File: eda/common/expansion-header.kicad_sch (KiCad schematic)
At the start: 10 parts, among them J1 Bus expansion

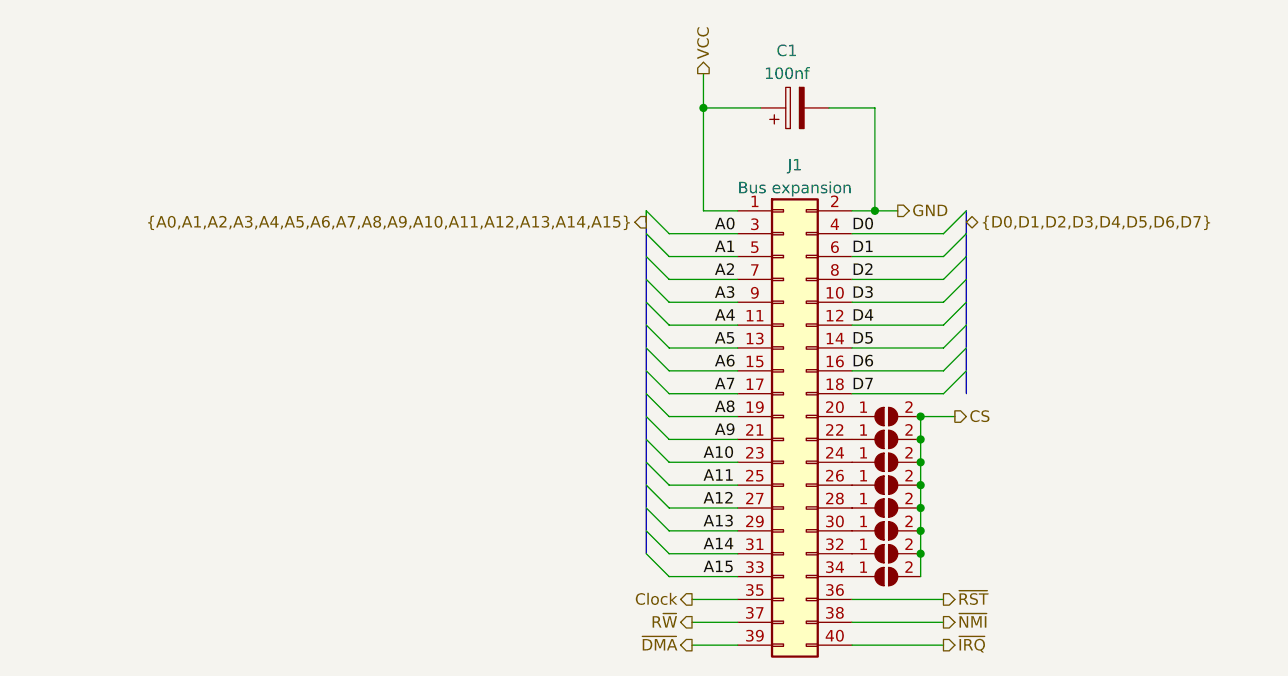
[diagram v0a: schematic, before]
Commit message: More work on UART
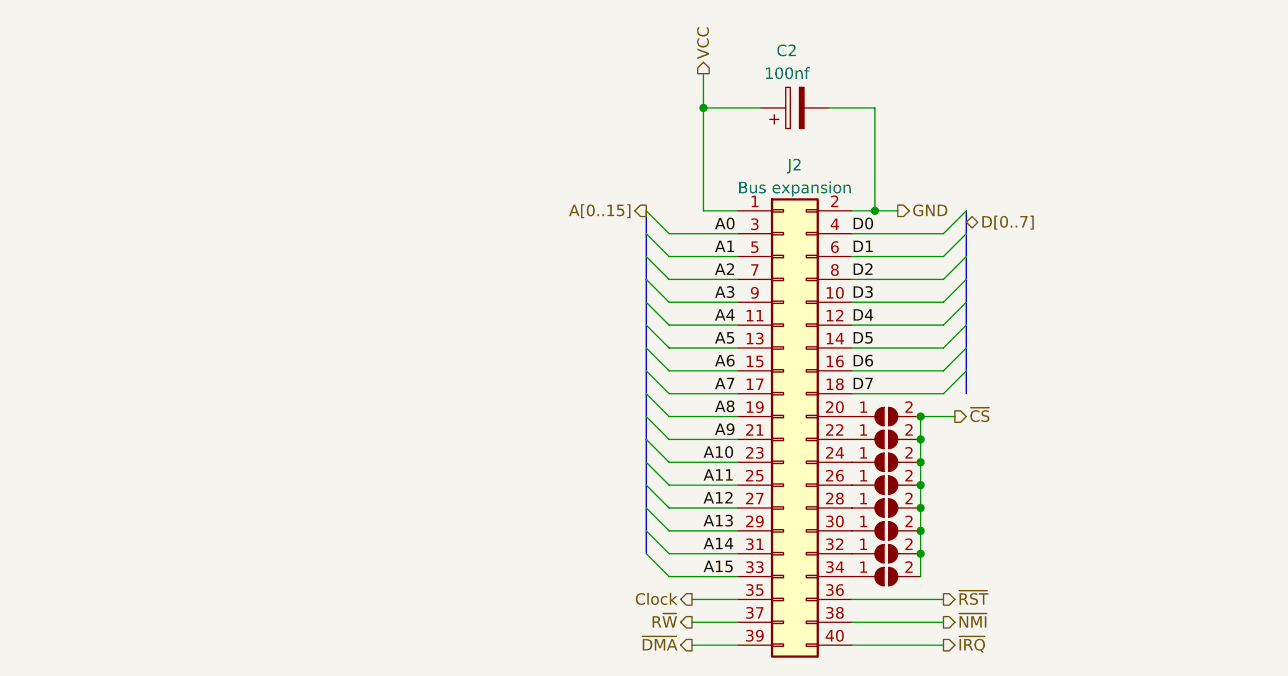
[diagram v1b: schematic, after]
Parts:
- renumbered C1 to C2, J1 to J2
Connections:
- net CS renamed ~{CS}

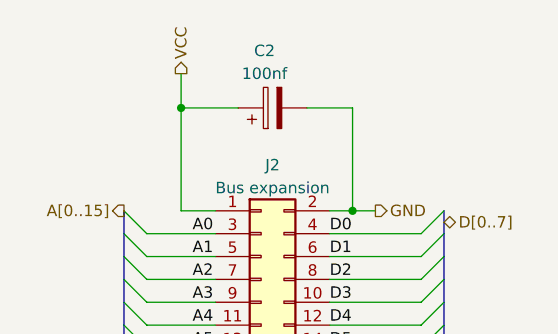
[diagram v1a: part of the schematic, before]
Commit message: Port main board schematic to kicad
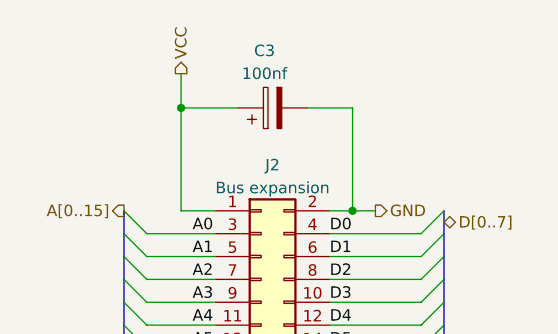
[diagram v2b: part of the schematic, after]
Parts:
- renumbered C2 to C3
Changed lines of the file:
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@@
   (symbol (lib_id "Device:C_Polarized") (at 90.17 38.1 90) (unit 1)
     (in_bom yes) (on_board yes) (dnp no) (fields_autoplaced)
-    (property "Reference" "C2" (at 89.281 31.75 90)
+    (property "Reference" "C3" (at 89.281 31.75 90)
       (effects (font (size 1.27 1.27)))
     )
@@
       (project "uart"
         (path "/11545594-d6d6-4b37-a578-fa23933d5773/07300109-a3a2-4acb-97d9-cd917026a3f9"
-          (reference "C2") (unit 1)
+          (reference "C3") (unit 1)
         )
       )

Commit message: Work on main board eda, interim
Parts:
- renumbered C3 to C18
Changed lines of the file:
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@@
     (pin "9")
     (instances
-      (project "uart"
-        (path "/11545594-d6d6-4b37-a578-fa23933d5773/07300109-a3a2-4acb-97d9-cd917026a3f9"
+      (project "fpga_gpu"
+        (path "/1109c9a4-a9ef-4407-8781-29fe7740bcaf/e520acf4-60a8-4598-8dc0-60738d0b1043/67c1a8cf-e42b-4097-97dd-eb2d8cef1b43"
           (reference "J2") (unit 1)
         )
       )
+      (project "uart"
+        (path "/11545594-d6d6-4b37-a578-fa23933d5773/07300109-a3a2-4acb-97d9-cd917026a3f9"
+          (reference "J2") (unit 1)
+        )
+      )
     )
   )
@@
     (pin "2")
     (instances
-      (project "uart"
-        (path "/11545594-d6d6-4b37-a578-fa23933d5773/07300109-a3a2-4acb-97d9-cd917026a3f9"
+      (project "fpga_gpu"
+        (path "/1109c9a4-a9ef-4407-8781-29fe7740bcaf/e520acf4-60a8-4598-8dc0-60738d0b1043/67c1a8cf-e42b-4097-97dd-eb2d8cef1b43"
           (reference "JP3") (unit 1)
         )
       )
+      (project "uart"
+        (path "/11545594-d6d6-4b37-a578-fa23933d5773/07300109-a3a2-4acb-97d9-cd917026a3f9"
+          (reference "JP3") (unit 1)
+        )
+      )
     )
   )
@@
     (pin "2")
     (instances
-      (project "uart"
-        (path "/11545594-d6d6-4b37-a578-fa23933d5773/07300109-a3a2-4acb-97d9-cd917026a3f9"
+      (project "fpga_gpu"
+        (path "/1109c9a4-a9ef-4407-8781-29fe7740bcaf/e520acf4-60a8-4598-8dc0-60738d0b1043/67c1a8cf-e42b-4097-97dd-eb2d8cef1b43"
           (reference "JP5") (unit 1)
         )
       )
+      (project "uart"
+        (path "/11545594-d6d6-4b37-a578-fa23933d5773/07300109-a3a2-4acb-97d9-cd917026a3f9"
+          (reference "JP5") (unit 1)
+        )
+      )
     )
   )
@@
     (pin "2")
     (instances
-      (project "uart"
-        (path "/11545594-d6d6-4b37-a578-fa23933d5773/07300109-a3a2-4acb-97d9-cd917026a3f9"
+      (project "fpga_gpu"
+        (path "/1109c9a4-a9ef-4407-8781-29fe7740bcaf/e520acf4-60a8-4598-8dc0-60738d0b1043/67c1a8cf-e42b-4097-97dd-eb2d8cef1b43"
           (reference "JP7") (unit 1)
         )
       )
+      (project "uart"
+        (path "/11545594-d6d6-4b37-a578-fa23933d5773/07300109-a3a2-4acb-97d9-cd917026a3f9"
+          (reference "JP7") (unit 1)
+        )
+      )
     )
   )
@@
     (pin "2")
     (instances
-      (project "uart"
-        (path "/11545594-d6d6-4b37-a578-fa23933d5773/07300109-a3a2-4acb-97d9-cd917026a3f9"
+      (project "fpga_gpu"
+        (path "/1109c9a4-a9ef-4407-8781-29fe7740bcaf/e520acf4-60a8-4598-8dc0-60738d0b1043/67c1a8cf-e42b-4097-97dd-eb2d8cef1b43"
           (reference "JP4") (unit 1)
         )
       )
+      (project "uart"
+        (path "/11545594-d6d6-4b37-a578-fa23933d5773/07300109-a3a2-4acb-97d9-cd917026a3f9"
+          (reference "JP4") (unit 1)
+        )
+      )
     )
   )
@@
     (pin "2")
     (instances
-      (project "uart"
-        (path "/11545594-d6d6-4b37-a578-fa23933d5773/07300109-a3a2-4acb-97d9-cd917026a3f9"
+      (project "fpga_gpu"
+        (path "/1109c9a4-a9ef-4407-8781-29fe7740bcaf/e520acf4-60a8-4598-8dc0-60738d0b1043/67c1a8cf-e42b-4097-97dd-eb2d8cef1b43"
           (reference "JP2") (unit 1)
         )
       )
+      (project "uart"
+        (path "/11545594-d6d6-4b37-a578-fa23933d5773/07300109-a3a2-4acb-97d9-cd917026a3f9"
+          (reference "JP2") (unit 1)
+        )
+      )
     )
   )
@@
     (pin "2")
     (instances
-      (project "uart"
-        (path "/11545594-d6d6-4b37-a578-fa23933d5773/07300109-a3a2-4acb-97d9-cd917026a3f9"
+      (project "fpga_gpu"
+        (path "/1109c9a4-a9ef-4407-8781-29fe7740bcaf/e520acf4-60a8-4598-8dc0-60738d0b1043/67c1a8cf-e42b-4097-97dd-eb2d8cef1b43"
           (reference "JP6") (unit 1)
         )
       )
+      (project "uart"
+        (path "/11545594-d6d6-4b37-a578-fa23933d5773/07300109-a3a2-4acb-97d9-cd917026a3f9"
+          (reference "JP6") (unit 1)
+        )
+      )
     )
   )
@@
     (pin "2")
     (instances
-      (project "uart"
-        (path "/11545594-d6d6-4b37-a578-fa23933d5773/07300109-a3a2-4acb-97d9-cd917026a3f9"
+      (project "fpga_gpu"
+        (path "/1109c9a4-a9ef-4407-8781-29fe7740bcaf/e520acf4-60a8-4598-8dc0-60738d0b1043/67c1a8cf-e42b-4097-97dd-eb2d8cef1b43"
           (reference "JP8") (unit 1)
         )
       )
+      (project "uart"
+        (path "/11545594-d6d6-4b37-a578-fa23933d5773/07300109-a3a2-4acb-97d9-cd917026a3f9"
+          (reference "JP8") (unit 1)
+        )
+      )
     )
   )
   (symbol (lib_id "Device:C_Polarized") (at 90.17 38.1 90) (unit 1)
     (in_bom yes) (on_board yes) (dnp no) (fields_autoplaced)
-    (property "Reference" "C3" (at 89.281 31.75 90)
+    (property "Reference" "C18" (at 89.281 31.75 90)
       (effects (font (size 1.27 1.27)))
     )
@@
     (pin "2")
     (instances
+      (project "fpga_gpu"
+        (path "/1109c9a4-a9ef-4407-8781-29fe7740bcaf/e520acf4-60a8-4598-8dc0-60738d0b1043/67c1a8cf-e42b-4097-97dd-eb2d8cef1b43"
+          (reference "C18") (unit 1)
+        )
+      )
       (project "uart"
         (path "/11545594-d6d6-4b37-a578-fa23933d5773/07300109-a3a2-4acb-97d9-cd917026a3f9"
@@
     (pin "2")
     (instances
-      (project "uart"
-        (path "/11545594-d6d6-4b37-a578-fa23933d5773/07300109-a3a2-4acb-97d9-cd917026a3f9"
+      (project "fpga_gpu"
+        (path "/1109c9a4-a9ef-4407-8781-29fe7740bcaf/e520acf4-60a8-4598-8dc0-60738d0b1043/67c1a8cf-e42b-4097-97dd-eb2d8cef1b43"
+          (reference "JP1") (unit 1)
+        )
+      )
+      (project "uart"
+        (path "/11545594-d6d6-4b37-a578-fa23933d5773/07300109-a3a2-4acb-97d9-cd917026a3f9"

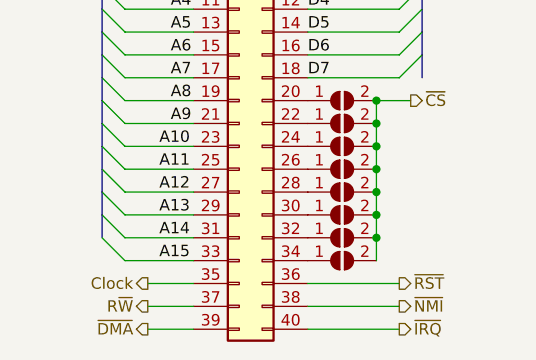
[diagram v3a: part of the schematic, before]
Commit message: More routing on the GPU board
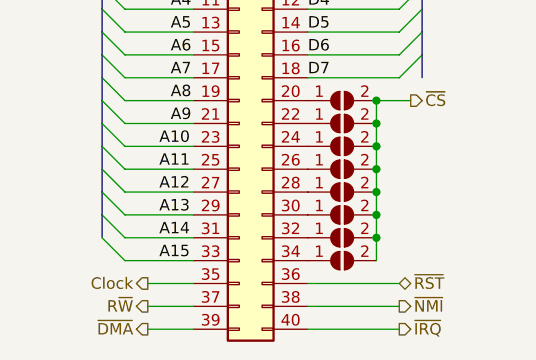
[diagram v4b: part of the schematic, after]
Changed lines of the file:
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@@
     (effects (font (size 1.27 1.27)) (justify right))
   )
-  (hierarchical_label "~{RST}" (shape output) (at 106.68 92.71 0) (fields_autoplaced)
+  (hierarchical_label "~{RST}" (shape bidirectional) (at 106.68 92.71 0) (fields_autoplaced)
     (effects (font (size 1.27 1.27)) (justify left))
   )

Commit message: Convert expansion breakout to kicad
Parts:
- J2: footprint Connector_PinHeader_2.54mm:PinHeader_2x20_P2.54mm_Vertical -> Connector_PinHeader_2.54mm:PinHeader_2x20_P2.54mm_Horizontal
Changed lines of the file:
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@@
       (effects (font (size 1.27 1.27)))
     )
-    (property "Footprint" "Connector_PinHeader_2.54mm:PinHeader_2x20_P2.54mm_Vertical" (at 88.9 72.39 0)
+    (property "Footprint" "Connector_PinHeader_2.54mm:PinHeader_2x20_P2.54mm_Horizontal" (at 88.9 72.39 0)
       (effects (font (size 1.27 1.27)) hide)
     )
@@
         )
       )
+      (project "expansion_skeleton"
+        (path "/f65326c0-118f-43ae-8d7d-86cc11609fcf/a49eac83-5c79-4825-9699-833a4117337f"
+          (reference "J2") (unit 1)
+        )
+      )
     )
   )
@@
         )
       )
+      (project "expansion_skeleton"
+        (path "/f65326c0-118f-43ae-8d7d-86cc11609fcf/a49eac83-5c79-4825-9699-833a4117337f"
+          (reference "JP3") (unit 1)
+        )
+      )
     )
   )
@@
         )
       )
+      (project "expansion_skeleton"
+        (path "/f65326c0-118f-43ae-8d7d-86cc11609fcf/a49eac83-5c79-4825-9699-833a4117337f"
+          (reference "JP5") (unit 1)
+        )
+      )
     )
   )
@@
         )
       )
+      (project "expansion_skeleton"
+        (path "/f65326c0-118f-43ae-8d7d-86cc11609fcf/a49eac83-5c79-4825-9699-833a4117337f"
+          (reference "JP7") (unit 1)
+        )
+      )
     )
   )
@@
         )
       )
+      (project "expansion_skeleton"
+        (path "/f65326c0-118f-43ae-8d7d-86cc11609fcf/a49eac83-5c79-4825-9699-833a4117337f"
+          (reference "JP4") (unit 1)
+        )
+      )
     )
   )
@@
         )
       )
+      (project "expansion_skeleton"
+        (path "/f65326c0-118f-43ae-8d7d-86cc11609fcf/a49eac83-5c79-4825-9699-833a4117337f"
+          (reference "JP2") (unit 1)
+        )
+      )
     )
   )
@@
         )
       )
+      (project "expansion_skeleton"
+        (path "/f65326c0-118f-43ae-8d7d-86cc11609fcf/a49eac83-5c79-4825-9699-833a4117337f"
+          (reference "JP6") (unit 1)
+        )
+      )
     )
   )
@@
       (project "io-card"
         (path "/88a1e5ee-bcfe-4f55-a7a9-4b7b5eaf475b/5d80791e-4732-481b-8542-898a0c887aef"
+          (reference "JP8") (unit 1)
+        )
+      )
+      (project "expansion_skeleton"
+        (path "/f65326c0-118f-43ae-8d7d-86cc11609fcf/a49eac83-5c79-4825-9699-833a4117337f"
           (reference "JP8") (unit 1)
         )
@@
         )
       )
+      (project "expansion_skeleton"
+        (path "/f65326c0-118f-43ae-8d7d-86cc11609fcf/a49eac83-5c79-4825-9699-833a4117337f"
+          (reference "C18") (unit 1)
+        )
+      )
     )
   )
@@
           (reference "JP1") (unit 1)
         )
+      )
+      (project "expansion_skeleton"
+        (path "/f65326c0-118f-43ae-8d7d-86cc11609fcf/a49eac83-5c79-4825-9699-833a4117337f"
+          (reference "JP1") (unit 1)
+        )
